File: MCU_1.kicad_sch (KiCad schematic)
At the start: 21 parts, among them J5 JLink-1, J6 JLink-2, J7 Conn_02x20, J8 Conn_02x20, SW1 SW_SPST, SW2 SW_SPST, U2 LPC55S28JBD100, Y1 16MHz

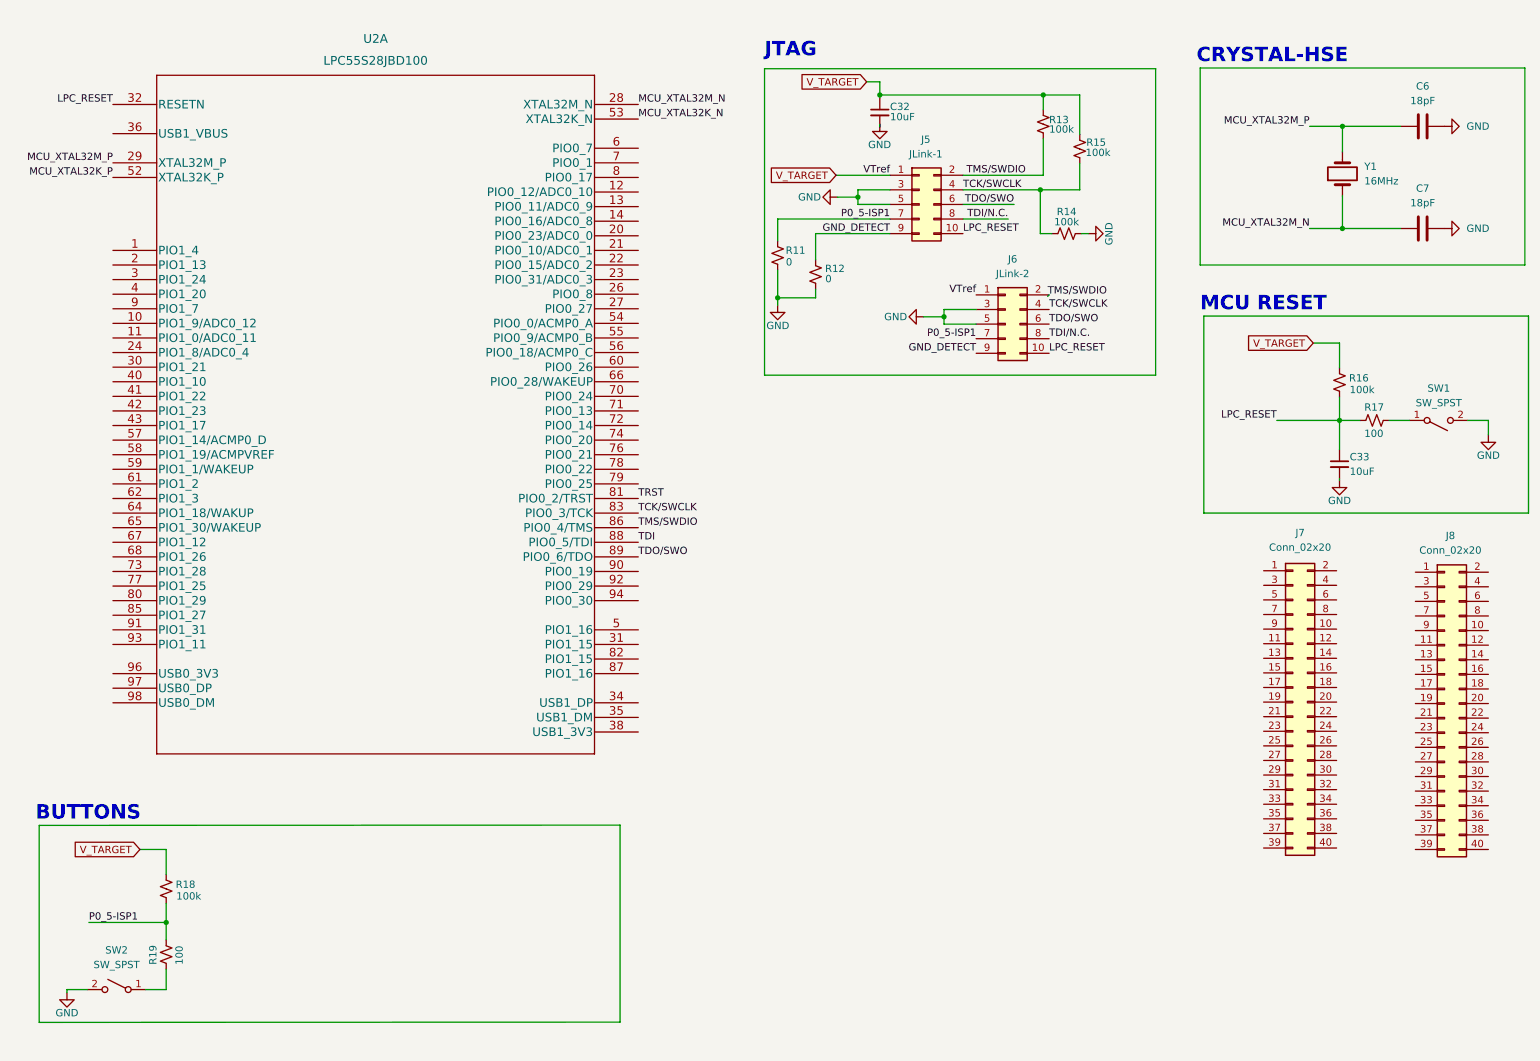
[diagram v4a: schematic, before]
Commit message: JTAG swo pin pull down yapıldı
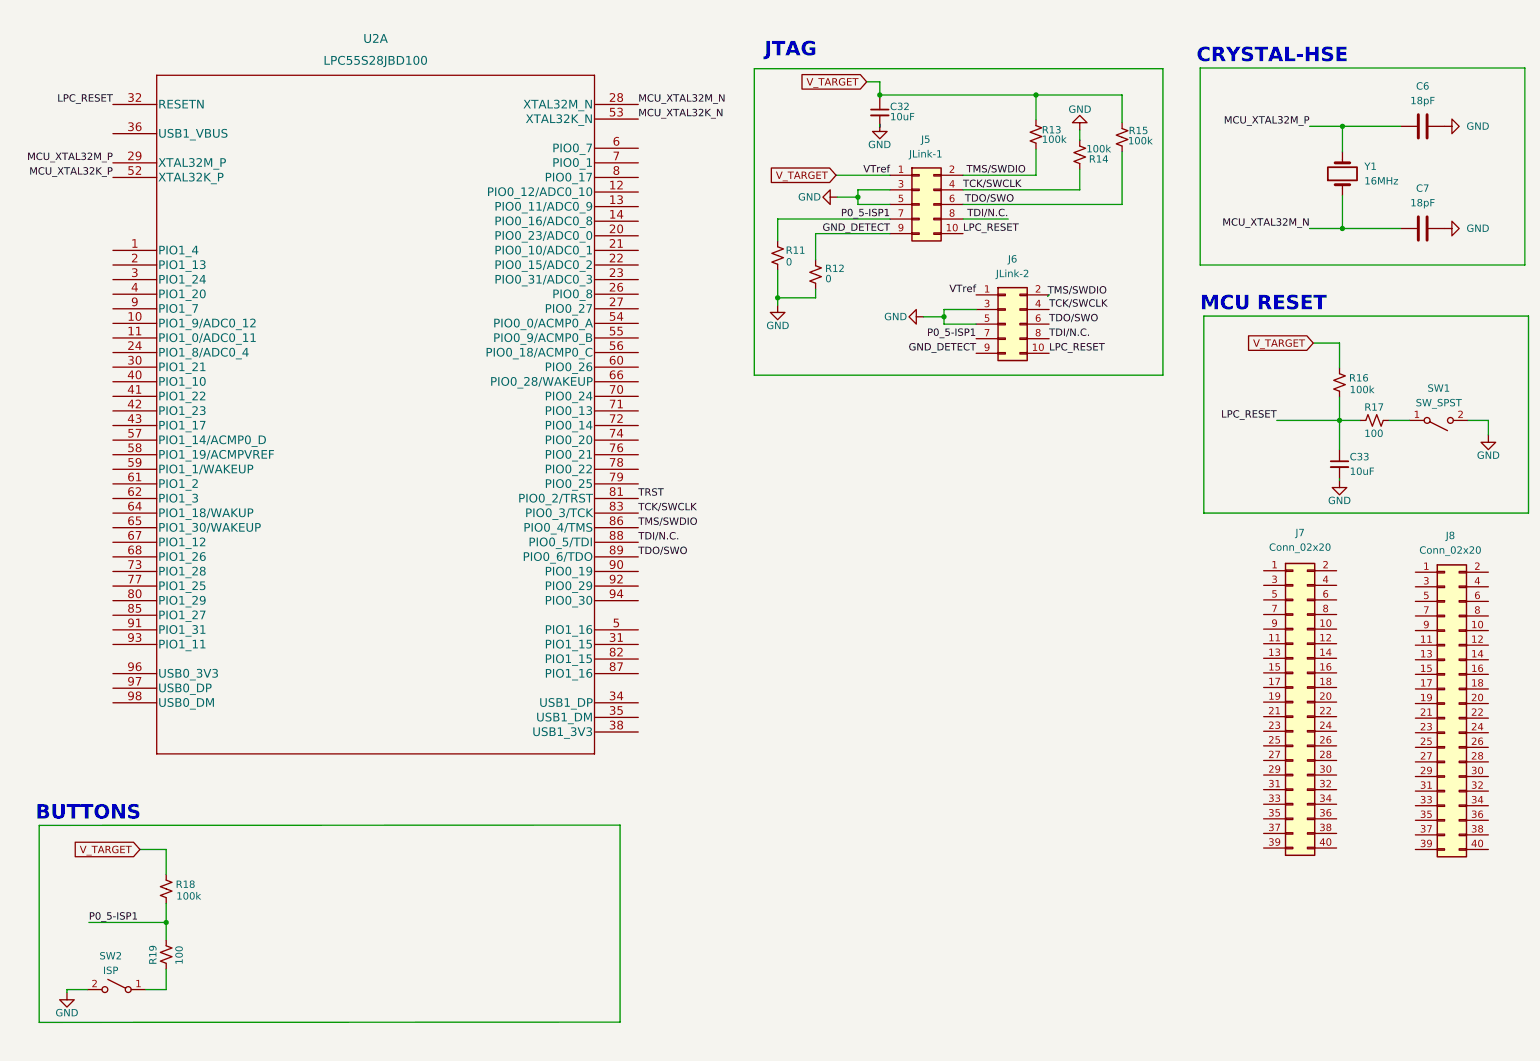
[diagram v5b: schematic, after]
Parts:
- SW2: value SW_SPST -> ISP
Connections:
- net TDI is gone; now on net TDI/N.C.: U2.88 (PIO0_5/TDI)
- net TCK/SWCLK: no longer R15.1
- net TDO/SWO: now also R15.1
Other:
- moved on the sheet: R13, R14, R15

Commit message: Butonlar eklendi
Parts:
- removed R19: 100, Resistor_SMD:R_0603_1608Metric, symbol Device:R_Small_US
- added R12: 330k, Resistor_SMD:R_0603_1608Metric, symbol Device:R_Small_US
- added R13, R18: 100k, Resistor_SMD:R_0603_1608Metric, symbol Device:R_Small_US
- added R14: 100, Resistor_SMD:R_0603_1608Metric, symbol Device:R_Small_US
- added SW1: ISP, Button_Switch_SMD:SW_SPST_PTS645, symbol Switch:SW_SPST
- added SW3: USER, Button_Switch_SMD:SW_SPST_PTS645, symbol Switch:SW_SPST
- R11: renamed from R18; value 100k -> 2.2k
- SW2: value ISP -> WAKE
- renumbered C32 to C30, C33 to C31, C6 to C32, C7 to C33, J5 to J6, J6 to J7, J7 to J8, J8 to J9, R11 to R15, R12 to R16, R13 to R17, R14 to R19, R15 to R20, R16 to R21, R17 to R22, SW1 to SW4, U2 to U5
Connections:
- net GND: now also SW2.1 (A), R18.2, SW1.1 (A), SW3.1 (A); no longer SW2.2 (B)
- net P0_5-ISP1: now also SW1.2 (B)
- net TDI/N.C.: now also R18.1
- net V_TARGET: now also R12.1, R13.1
- net WAKE/GPIO: now reaches U5.64 (PIO1_18/WAKUP)
- net WAKE/GPIO: now also SW2.2 (B), R12.2
- new net: R14.2, SW3.2 (B)
- new net PIO1_9: R13.2, R14.1
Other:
- moved on the sheet: J7, R11, U5A

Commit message: Butonlar eklendi ve usb eklendi
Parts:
- added J6, J7: USB_B_Micro, Connector_USB:USB_Micro-B_Molex_47346-0001, symbol Connector:USB_B_Micro
- renumbered J8 to J10, J9 to J11, J6 to J8, J7 to J9
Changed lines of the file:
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@@
   (symbol (lib_id "Connector_Generic:Conn_02x05_Odd_Even") (at 185.039 68.58 0) (unit 1)
     (in_bom yes) (on_board yes) (fields_autoplaced)
-    (property "Reference" "J7" (id 0) (at 186.309 57.277 0))
+    (property "Reference" "J9" (id 0) (at 186.309 57.277 0))
     (property "Value" "JLink-2" (id 1) (at 186.309 59.817 0))
     (property "Footprint" "Connector_IDC:IDC-Header_2x05_P2.54mm_Vertical" (id 2) (at 185.039 68.58 0)
@@
   (symbol (lib_id "Connector_Generic:Conn_02x20_Odd_Even") (at 265.43 134.112 0) (unit 1)
     (in_bom yes) (on_board yes)
-    (property "Reference" "J9" (id 0) (at 266.446 104.902 0))
+    (property "Reference" "J11" (id 0) (at 266.446 104.902 0))
     (property "Value" "Conn_02x20" (id 1) (at 266.446 107.442 0))
     (property "Footprint" "Connector_PinSocket_2.54mm:PinSocket_2x20_P2.54mm_Vertical" (id 2) (at 265.43 134.112 0)
@@
   (symbol (lib_id "Connector_Generic:Conn_02x05_Odd_Even") (at 173.99 47.244 0) (unit 1)
     (in_bom yes) (on_board yes)
-    (property "Reference" "J6" (id 0) (at 175.133 35.941 0))
+    (property "Reference" "J8" (id 0) (at 175.133 35.941 0))
     (property "Value" "JLink-1" (id 1) (at 175.133 38.481 0))
     (property "Footprint" "Connector_PinHeader_1.27mm:PinHeader_2x05_P1.27mm_Vertical" (id 2) (at 173.99 47.244 0)
@@
     (pin "2")
   )
+  (symbol (lib_id "Connector:USB_B_Micro") (at 160.528 113.284 0) (unit 1)
+    (in_bom yes) (on_board yes) (fields_autoplaced)
+    (property "Reference" "J7" (id 0) (at 160.528 100.584 0))
+    (property "Value" "USB_B_Micro" (id 1) (at 160.528 103.124 0))
+    (property "Footprint" "Connector_USB:USB_Micro-B_Molex_47346-0001" (id 2) (at 164.338 114.554 0)
+      (effects (font (size 1.27 1.27)) hide)
+    )
+    (property "Datasheet" "~" (id 3) (at 164.338 114.554 0)
+      (effects (font (size 1.27 1.27)) hide)
+    )
+    (pin "1")
+    (pin "2")
+    (pin "3")
+    (pin "4")
+    (pin "5")
+    (pin "6")
+  )
   (symbol (lib_id "Device:C_Small") (at 167.132 31.242 0) (unit 1)
     (in_bom yes) (on_board yes)
@@
   (symbol (lib_id "Connector_Generic:Conn_02x20_Odd_Even") (at 239.014 133.858 0) (unit 1)
     (in_bom yes) (on_board yes)
-    (property "Reference" "J8" (id 0) (at 240.284 104.394 0))
+    (property "Reference" "J10" (id 0) (at 240.284 104.394 0))
     (property "Value" "Conn_02x20" (id 1) (at 240.284 106.934 0))
     (property "Footprint" "Connector_PinSocket_2.54mm:PinSocket_2x20_P2.54mm_Vertical" (id 2) (at 239.014 133.858 0)
@@
     (pin "1")
   )
+  (symbol (lib_id "Connector:USB_B_Micro") (at 160.274 152.4 0) (unit 1)
+    (in_bom yes) (on_board yes) (fields_autoplaced)
+    (property "Reference" "J6" (id 0) (at 160.274 139.7 0))
+    (property "Value" "USB_B_Micro" (id 1) (at 160.274 142.24 0))
+    (property "Footprint" "Connector_USB:USB_Micro-B_Molex_47346-0001" (id 2) (at 164.084 153.67 0)
+      (effects (font (size 1.27 1.27)) hide)
+    )
+    (property "Datasheet" "~" (id 3) (at 164.084 153.67 0)
+      (effects (font (size 1.27 1.27)) hide)
+    )
+    (pin "1")
+    (pin "2")
+    (pin "3")
+    (pin "4")
+    (pin "5")
+    (pin "6")
+  )
   (symbol (lib_id "Device:C_Small") (at 247.142 92.456 0) (unit 1)

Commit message: Pin labelları eklendi
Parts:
- SW4: value SW_SPST -> MCU_RESET
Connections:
- net P1_4: now reaches U5.1 (PIO1_4)
- net P1_9: now reaches U5.10 (PIO1_9/ADC0_12)
- net P1_0: now reaches U5.11 (PIO1_0/ADC0_11)
- net P0_12: now reaches U5.12 (PIO0_12/ADC0_10)
- net P0_11: now reaches U5.13 (PIO0_11/ADC0_9)
- net P0_16: now reaches U5.14 (PIO0_16/ADC0_8)
- net P0_16: now also U5.22 (PIO0_15/ADC0_2)
- net P1_13: now reaches U5.2 (PIO1_13)
- net P0_23: now reaches U5.20 (PIO0_23/ADC0_0)
- net P0_10: now reaches U5.21 (PIO0_10/ADC0_1)
- net P0_31: now reaches U5.23 (PIO0_31/ADC0_3)
- net P1_8: now reaches U5.24 (PIO1_8/ADC0_4)
- net P0_8: now reaches U5.26 (PIO0_8)
- net P0_27: now reaches U5.27 (PIO0_27)
- net P1_24: now reaches U5.3 (PIO1_24)
- net P1_21: now reaches U5.30 (PIO1_21)
- net P1_15: now reaches U5.31 (PIO1_15)
- net P1_15: now also U5.82 (PIO1_15)
- net P1_20: now reaches U5.4 (PIO1_20)
- net P1_10: now reaches U5.40 (PIO1_10)
- net P1_22: now reaches U5.41 (PIO1_22)
- net P1_23: now reaches U5.42 (PIO1_23)
- net P1_17: now reaches U5.43 (PIO1_17)
- net P1_16: now reaches U5.5 (PIO1_16)
- net P1_16: now also U5.87 (PIO1_16)
- net P0_0: now reaches U5.54 (PIO0_0/ACMP0_A)
- net P0_9: now reaches U5.55 (PIO0_9/ACMP0_B)
- net P0_18: now reaches U5.56 (PIO0_18/ACMP0_C)
- net P1_14: now reaches U5.57 (PIO1_14/ACMP0_D)
- net P1_19: now reaches U5.58 (PIO1_19/ACMPVREF)
- net P1_1: now reaches U5.59 (PIO1_1/WAKEUP)
- net P0_7: now reaches U5.6 (PIO0_7)
- net P0_7: now also U5.8 (PIO0_17)
- net P0_26: now reaches U5.60 (PIO0_26)
- net P1_2: now reaches U5.61 (PIO1_2)
- net P1_3: now reaches U5.62 (PIO1_3)
- net P1_30: now reaches U5.65 (PIO1_30/WAKEUP)
- net P0_28: now reaches U5.66 (PIO0_28/WAKEUP)
- net P1_12: now reaches U5.67 (PIO1_12)
- net P1_26: now reaches U5.68 (PIO1_26)
- net P0_1: now reaches U5.7 (PIO0_1)
- net P0_24: now reaches U5.70 (PIO0_24)
- net P0_13: now reaches U5.71 (PIO0_13)
- net P0_14: now reaches U5.72 (PIO0_14)
- net P1_28: now reaches U5.73 (PIO1_28)
- net P0_20: now reaches U5.74 (PIO0_20)
- net P0_21: now reaches U5.76 (PIO0_21)
- net P1_25: now reaches U5.77 (PIO1_25)
- net P0_22: now reaches U5.78 (PIO0_22)
- net P0_25: now reaches U5.79 (PIO0_25)
- net P1_29: now reaches U5.80 (PIO1_29)
- net P1_27: now reaches U5.85 (PIO1_27)
- net P1_7: now reaches U5.9 (PIO1_7)
- net P0_19: now reaches U5.90 (PIO0_19)
- net P1_31: now reaches U5.91 (PIO1_31)
- net P0_29: now reaches U5.92 (PIO0_29)
- net P1_11: now reaches U5.93 (PIO1_11)
- net P0_30: now reaches U5.94 (PIO0_30)
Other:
- moved on the sheet: J6, J7, SW4
